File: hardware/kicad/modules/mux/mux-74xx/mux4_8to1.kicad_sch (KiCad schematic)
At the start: 8 parts, among them U242 74LS151, U243 74LS151, U244 74LS151, U245 74LS151

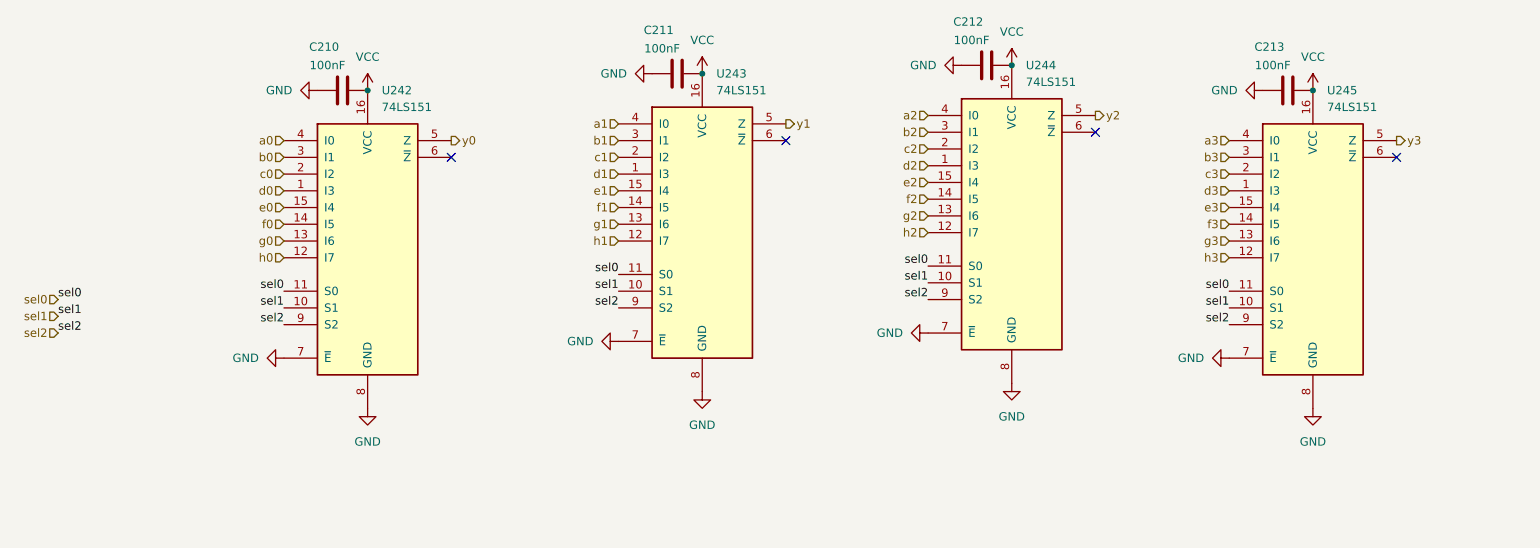
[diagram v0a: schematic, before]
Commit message: refactor: improved driver with data bus for readability
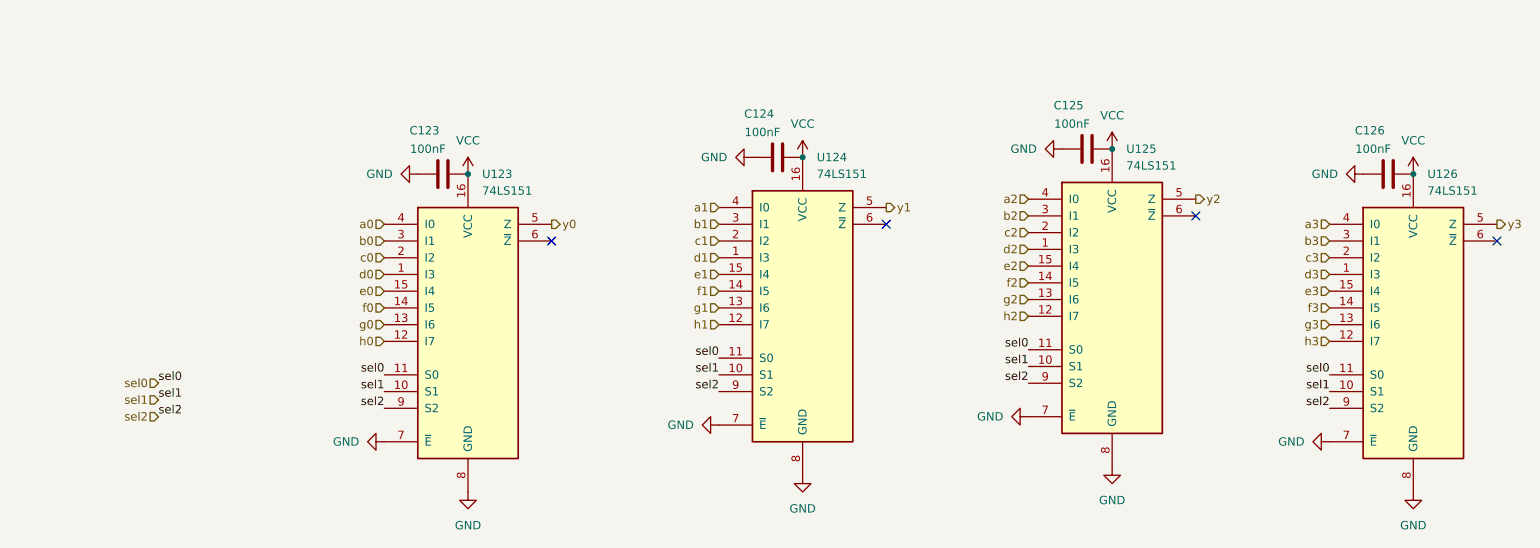
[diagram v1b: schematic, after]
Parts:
- removed C210, C211, C212, C213: 100nF, Capacitor_SMD:C_0805_2012Metric, symbol Device:C
- removed U242, U243, U244, U245: 74LS151, Package_SO:SOIC-16_3.9x9.9mm_P1.27mm, symbol 74xx:74LS151
- added C123, C124, C125, C126: 100nF, Capacitor_SMD:C_0805_2012Metric, symbol Device:C
- added U123, U124, U125, U126: 74LS151, Package_SO:SOIC-16_3.9x9.9mm_P1.27mm, symbol 74xx:74LS151
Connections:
- net GND: now also C123.1, C124.1, C125.1, C126.1, U123.7 (~{E}), U123.8 (GND), U124.7 (~{E}), U124.8 (GND), U125.7 (~{E}), U125.8 (GND), U126.7 (~{E}), U126.8 (GND)
- net VCC: now also C123.2, C124.2, C125.2, C126.2, U123.16 (VCC), U124.16 (VCC), U125.16 (VCC), U126.16 (VCC)
- net a0: now also U123.4 (I0)
- net a1: now also U124.4 (I0)
- net a2: now also U125.4 (I0)
- net a3: now also U126.4 (I0)
- net b0: now also U123.3 (I1)
- net b1: now also U124.3 (I1)
- net b2: now also U125.3 (I1)
- net b3: now also U126.3 (I1)
- net c0: now also U123.2 (I2)
- net c1: now also U124.2 (I2)
- net c2: now also U125.2 (I2)
- net c3: now also U126.2 (I2)
- net d0: now also U123.1 (I3)
- net d1: now also U124.1 (I3)
- net d2: now also U125.1 (I3)
- net d3: now also U126.1 (I3)
- net e0: now also U123.15 (I4)
- net e1: now also U124.15 (I4)
- net e2: now also U125.15 (I4)
- net e3: now also U126.15 (I4)
- net f0: now also U123.14 (I5)
- net f1: now also U124.14 (I5)
- net f2: now also U125.14 (I5)
- net f3: now also U126.14 (I5)
- net g0: now also U123.13 (I6)
- net g1: now also U124.13 (I6)
- net g2: now also U125.13 (I6)
- net g3: now also U126.13 (I6)
- net h0: now also U123.12 (I7)
- net h1: now also U124.12 (I7)
- net h2: now also U125.12 (I7)
- net h3: now also U126.12 (I7)
- net sel0: now also U123.11 (S0), U124.11 (S0), U125.11 (S0), U126.11 (S0)
- net sel1: now also U123.10 (S1), U124.10 (S1), U125.10 (S1), U126.10 (S1)
- net sel2: now also U123.9 (S2), U124.9 (S2), U125.9 (S2), U126.9 (S2)
- net y0: now also U123.5 (Z)
- net y1: now also U124.5 (Z)
- net y2: now also U125.5 (Z)
- net y3: now also U126.5 (Z)

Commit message: arch: added LEDs, override switches; fixed errors and warnings to 0
ready for routing after logical coherence check
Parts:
- renumbered C123 to C217, C124 to C218, C125 to C219, C126 to C220, U123 to U217, U124 to U218, U125 to U219, U126 to U220

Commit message: chore: modified muxes that alu depends on
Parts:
- renumbered C217 to C222, C218 to C223, C219 to C224, C220 to C225, U217 to U222, U218 to U223, U219 to U224, U220 to U225
